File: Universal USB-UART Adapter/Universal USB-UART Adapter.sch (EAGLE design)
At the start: 9 parts, among them U1 FT232RQ, X1 USBPCB

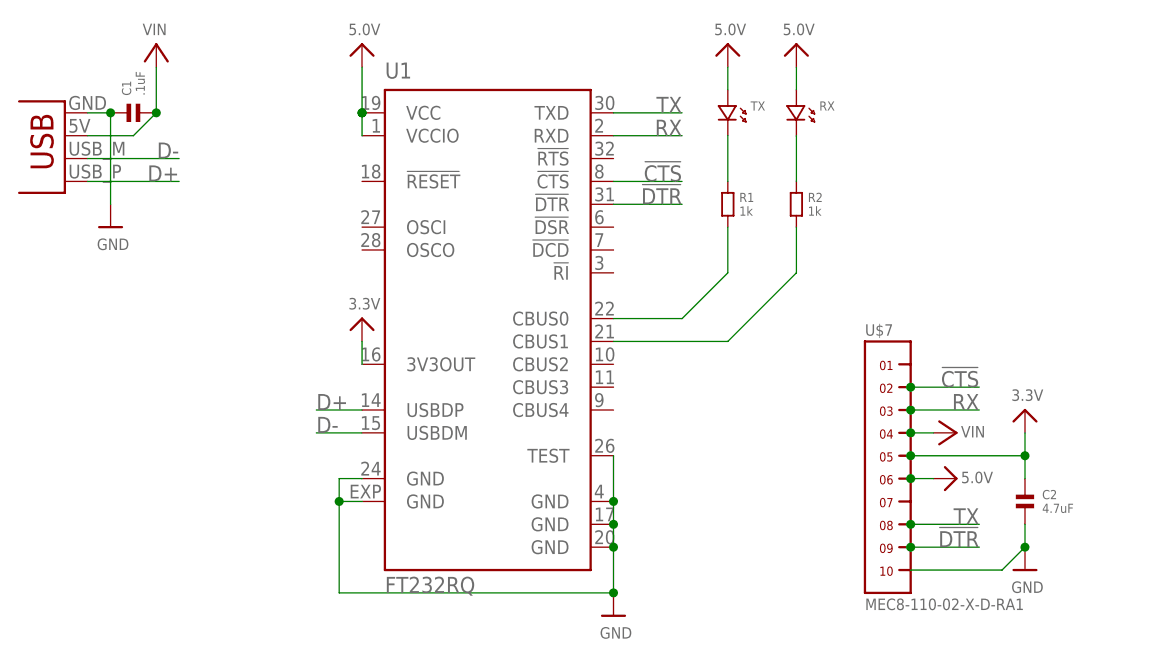
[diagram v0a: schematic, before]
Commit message: Modified voltage connections to be next to each other. Easier to short.
Signed-off-by: Cruz Monrreal II <Cruz.Monrreal@gmail.com>
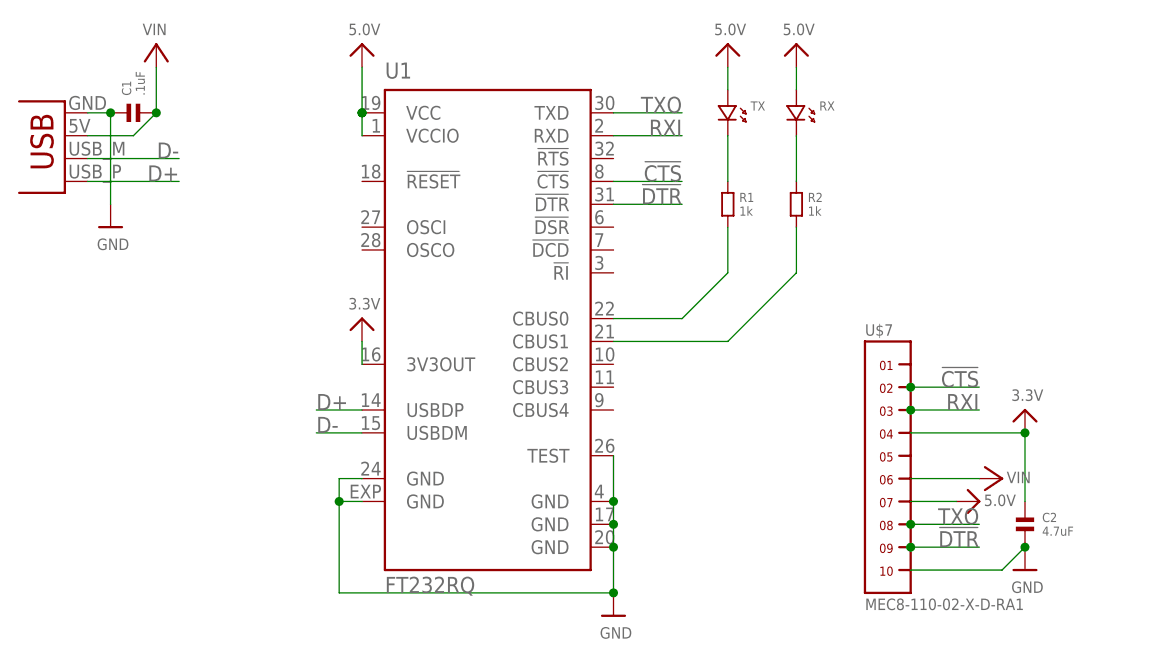
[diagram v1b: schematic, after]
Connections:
- net RX renamed RXI
- net TX renamed TXO
- net 3.3V: now also U$7.4; no longer U$7.5
- net 5.0V: now also U$7.7; no longer U$7.6
- net VIN: now also U$7.6; no longer U$7.4
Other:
- moved on the sheet: C2
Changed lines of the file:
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@@
 <instance part="TX" gate="G$1" x="93.98" y="154.94" rot="R270"/>
 <instance part="RX" gate="G$1" x="101.6" y="154.94" rot="R270"/>
-<instance part="U$3" gate="G$1" x="116.84" y="114.3" smashed="yes" rot="R270">
-<attribute name="VALUE" x="119.888" y="113.792" size="1.27" layer="96"/>
+<instance part="U$3" gate="G$1" x="119.38" y="111.76" smashed="yes" rot="R270">
+<attribute name="VALUE" x="122.428" y="111.252" size="1.27" layer="96"/>
 </instance>
 <instance part="C1" gate="G$1" x="27.94" y="154.94"/>
-<instance part="U$8" gate="G$1" x="116.84" y="119.38" smashed="yes" rot="R270">
-<attribute name="VALUE" x="119.888" y="118.872" size="1.27" layer="96"/>
+<instance part="U$8" gate="G$1" x="121.92" y="114.3" smashed="yes" rot="R270">
+<attribute name="VALUE" x="124.968" y="113.792" size="1.27" layer="96"/>
 </instance>
 <instance part="U$9" gate="G$1" x="30.48" y="160.02"/>
 <instance part="U$11" gate="G$1" x="127" y="119.38"/>
 <instance part="U$12" gate="G$1" x="127" y="104.14"/>
-<instance part="C2" gate="G$1" x="127" y="111.76" rot="R270"/>
+<instance part="C2" gate="G$1" x="127" y="109.22" rot="R270"/>
 </instances>
 <busses>
@@
 <wire x1="124.46" y1="104.14" x2="127" y2="106.68" width="0.1524" layer="91"/>
 <pinref part="C2" gate="G$1" pin="2"/>
-<wire x1="127" y1="106.68" x2="127" y2="109.22" width="0.1524" layer="91"/>
 <junction x="127" y="106.68"/>
 <pinref part="U$7" gate="G$1" pin="10"/>
@@
 </segment>
 </net>
-<net name="TX" class="0">
+<net name="TXO" class="0">
 <segment>
 <wire x1="81.28" y1="154.94" x2="88.9" y2="154.94" width="0.1524" layer="91"/>
@@
 </segment>
 </net>
-<net name="RX" class="0">
+<net name="RXI" class="0">
 <segment>
 <wire x1="88.9" y1="152.4" x2="81.28" y2="152.4" width="0.1524" layer="91"/>
@@
 <segment>
 <pinref part="U$11" gate="G$1" pin="3.3V"/>
-<wire x1="127" y1="116.84" x2="127" y2="119.38" width="0.1524" layer="91"/>
 <pinref part="C2" gate="G$1" pin="1"/>
-<wire x1="127" y1="114.3" x2="127" y2="116.84" width="0.1524" layer="91"/>
-<wire x1="127" y1="116.84" x2="114.3" y2="116.84" width="0.1524" layer="91"/>
-<junction x="127" y="116.84"/>
-<pinref part="U$7" gate="G$1" pin="5"/>
-<junction x="114.3" y="116.84"/>
+<wire x1="127" y1="111.76" x2="127" y2="119.38" width="0.1524" layer="91"/>
+<pinref part="U$7" gate="G$1" pin="4"/>
+<wire x1="114.3" y1="119.38" x2="127" y2="119.38" width="0.1524" layer="91"/>
+<junction x="127" y="119.38"/>
 </segment>
 <segment>
@@
 </segment>
 <segment>
-<wire x1="114.3" y1="114.3" x2="116.84" y2="114.3" width="0.1524" layer="91"/>
+<pinref part="U$7" gate="G$1" pin="7"/>
 <pinref part="U$3" gate="G$1" pin="5.0V"/>
-<pinref part="U$7" gate="G$1" pin="6"/>
-<junction x="114.3" y="114.3"/>
+<wire x1="114.3" y1="111.76" x2="119.38" y2="111.76" width="0.1524" layer="91"/>
 </segment>
 </net>
@@
 </segment>
 <segment>
+<pinref part="U$7" gate="G$1" pin="6"/>
 <pinref part="U$8" gate="G$1" pin="VIN"/>
-<pinref part="U$7" gate="G$1" pin="4"/>
-<junction x="114.3" y="119.38"/>
-<wire x1="114.3" y1="119.38" x2="116.84" y2="119.38" width="0.1524" layer="91"/>
-</segment>
-</net>
+<wire x1="114.3" y1="114.3" x2="121.92" y2="114.3" width="0.1524" layer="91"/>
+</segment>
+</net>

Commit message: Changed connector to 2mm pitch as opposed to PCB connector
Signed-off-by: Cruz Monrreal II <Cruz.Monrreal@gmail.com>
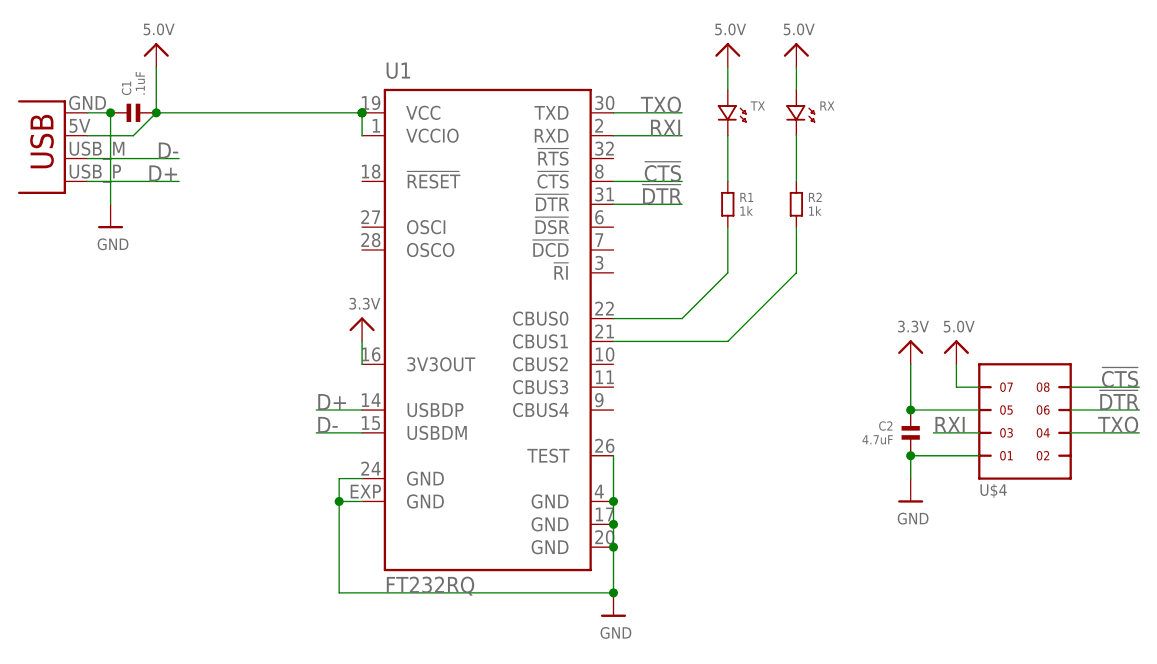
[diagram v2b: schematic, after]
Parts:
- removed U$7: MEC8-110-02-X-D-RA1, samtec:MEC8-110-02-X-D-RA1
- added U$4: (no value), samtec:MMT-104-01-X-DH-X
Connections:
- removed net VIN: C1.2, U$7.6, X1.VBUS
- net !CTS: now also U$4.8; no longer U$7.2
- net !DTR: now also U$4.6; no longer U$7.9
- net 3.3V: now also U$4.5; no longer U$7.4
- net 5.0V: now also C1.2, U$4.7, X1.VBUS; no longer U$7.7
- net GND: now also U$4.1; no longer U$7.10
- net RXI: now also U$4.3; no longer U$7.3
- net TXO: now also U$4.4; no longer U$7.8
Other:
- moved on the sheet: C2
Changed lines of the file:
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@@
 <part name="U$15" library="microbuilder" deviceset="5.0V" device=""/>
 <part name="U$6" library="microbuilder" deviceset="5.0V" device=""/>
-<part name="U$7" library="samtec" deviceset="MEC8-110-02-X-D-RA1" device=""/>
 <part name="R1" library=".standardparts" deviceset="RESISTOR" device=".0603" value="1k"/>
 <part name="R2" library=".standardparts" deviceset="RESISTOR" device=".0603" value="1k"/>
@@
 <part name="U$3" library="microbuilder" deviceset="5.0V" device=""/>
 <part name="C1" library=".standardparts" deviceset="CAPACITOR" device=".0603" value=".1uF"/>
-<part name="U$8" library="microbuilder" deviceset="VIN" device=""/>
-<part name="U$9" library="microbuilder" deviceset="VIN" device=""/>
 <part name="U$11" library="microbuilder" deviceset="3.3V" device=""/>
 <part name="U$12" library="microbuilder" deviceset="GND" device=""/>
 <part name="C2" library=".standardparts" deviceset="CAPACITOR" device=".0603" value="4.7uF"/>
+<part name="U$4" library="samtec" deviceset="MMT-104-01-X-DH-X" device=""/>
 </parts>
 <sheets>
@@
 <instance part="U$14" gate="G$1" x="101.6" y="160.02"/>
 <instance part="U$15" gate="G$1" x="93.98" y="160.02"/>
-<instance part="U$6" gate="G$1" x="53.34" y="160.02"/>
-<instance part="U$7" gate="G$1" x="111.76" y="116.84"/>
+<instance part="U$6" gate="G$1" x="30.48" y="160.02"/>
 <instance part="R1" gate="G$1" x="93.98" y="144.78" rot="R270"/>
 <instance part="R2" gate="G$1" x="101.6" y="144.78" rot="R270"/>
 <instance part="TX" gate="G$1" x="93.98" y="154.94" rot="R270"/>
 <instance part="RX" gate="G$1" x="101.6" y="154.94" rot="R270"/>
-<instance part="U$3" gate="G$1" x="119.38" y="111.76" smashed="yes" rot="R270">
-<attribute name="VALUE" x="122.428" y="111.252" size="1.27" layer="96"/>
+<instance part="U$3" gate="G$1" x="119.38" y="127"/>
+<instance part="C1" gate="G$1" x="27.94" y="154.94"/>
+<instance part="U$11" gate="G$1" x="114.3" y="127"/>
+<instance part="U$12" gate="G$1" x="114.3" y="111.76"/>
+<instance part="C2" gate="G$1" x="114.3" y="119.38" rot="MR270"/>
+<instance part="U$4" gate="G$1" x="127" y="121.92" smashed="yes" rot="MR180">
+<attribute name="NAME" x="121.92" y="113.665" size="1.27" layer="95" font="vector" rot="MR180"/>
+<attribute name="VALUE" x="121.92" y="128.905" size="1.27" layer="96" font="vector" rot="MR180"/>
 </instance>
-<instance part="C1" gate="G$1" x="27.94" y="154.94"/>
-<instance part="U$8" gate="G$1" x="121.92" y="114.3" smashed="yes" rot="R270">
-<attribute name="VALUE" x="124.968" y="113.792" size="1.27" layer="96"/>
-</instance>
-<instance part="U$9" gate="G$1" x="30.48" y="160.02"/>
-<instance part="U$11" gate="G$1" x="127" y="119.38"/>
-<instance part="U$12" gate="G$1" x="127" y="104.14"/>
-<instance part="C2" gate="G$1" x="127" y="109.22" rot="R270"/>
 </instances>
 <busses>
@@
 <segment>
 <pinref part="U$12" gate="G$1" pin="GND"/>
-<wire x1="114.3" y1="104.14" x2="124.46" y2="104.14" width="0.1524" layer="91"/>
-<wire x1="124.46" y1="104.14" x2="127" y2="106.68" width="0.1524" layer="91"/>
 <pinref part="C2" gate="G$1" pin="2"/>
-<junction x="127" y="106.68"/>
-<pinref part="U$7" gate="G$1" pin="10"/>
+<wire x1="114.3" y1="114.3" x2="114.3" y2="116.84" width="0.1524" layer="91"/>
+<pinref part="U$4" gate="G$1" pin="1"/>
+<wire x1="114.3" y1="116.84" x2="121.92" y2="116.84" width="0.1524" layer="91"/>
+<junction x="114.3" y="116.84"/>
 </segment>
 </net>
@@
 </segment>
 <segment>
-<wire x1="114.3" y1="109.22" x2="121.92" y2="109.22" width="0.1524" layer="91"/>
-<label x="121.92" y="109.22" size="1.778" layer="95" rot="MR0"/>
-<pinref part="U$7" gate="G$1" pin="8"/>
-<junction x="114.3" y="109.22"/>
+<wire x1="139.7" y1="119.38" x2="132.08" y2="119.38" width="0.1524" layer="91"/>
+<label x="139.7" y="119.38" size="1.778" layer="95" rot="MR0"/>
+<pinref part="U$4" gate="G$1" pin="4"/>
 </segment>
 </net>
@@
 </segment>
 <segment>
-<label x="121.92" y="121.92" size="1.778" layer="95" rot="MR0"/>
-<pinref part="U$7" gate="G$1" pin="3"/>
-<junction x="114.3" y="121.92"/>
-<wire x1="114.3" y1="121.92" x2="121.92" y2="121.92" width="0.1524" layer="91"/>
+<label x="116.84" y="119.38" size="1.778" layer="95"/>
+<wire x1="116.84" y1="119.38" x2="121.92" y2="119.38" width="0.1524" layer="91"/>
+<pinref part="U$4" gate="G$1" pin="3"/>
 </segment>
 </net>
 <net name="3.3V" class="0">
-<segment>
-<pinref part="U$11" gate="G$1" pin="3.3V"/>
-<pinref part="C2" gate="G$1" pin="1"/>
-<wire x1="127" y1="111.76" x2="127" y2="119.38" width="0.1524" layer="91"/>
-<pinref part="U$7" gate="G$1" pin="4"/>
-<wire x1="114.3" y1="119.38" x2="127" y2="119.38" width="0.1524" layer="91"/>
-<junction x="127" y="119.38"/>
-</segment>
 <segment>
 <pinref part="U1" gate="1" pin="3V3OUT"/>
@@
 <wire x1="53.34" y1="127" x2="53.34" y2="129.54" width="0.1524" layer="91"/>
 </segment>
+<segment>
+<pinref part="U$4" gate="G$1" pin="5"/>
+<wire x1="121.92" y1="121.92" x2="114.3" y2="121.92" width="0.1524" layer="91"/>
+<pinref part="U$11" gate="G$1" pin="3.3V"/>
+<wire x1="114.3" y1="121.92" x2="114.3" y2="127" width="0.1524" layer="91"/>
+<pinref part="C2" gate="G$1" pin="1"/>
+<junction x="114.3" y="121.92"/>
+</segment>
 </net>
 <net name="!DTR" class="0">
@@
 </segment>
 <segment>
-<wire x1="114.3" y1="106.68" x2="121.92" y2="106.68" width="0.1524" layer="91"/>
-<label x="121.92" y="106.68" size="1.778" layer="95" rot="MR0"/>
-<pinref part="U$7" gate="G$1" pin="9"/>
-<junction x="114.3" y="106.68"/>
+<wire x1="132.08" y1="121.92" x2="139.7" y2="121.92" width="0.1524" layer="91"/>
+<label x="139.7" y="121.92" size="1.778" layer="95" rot="MR0"/>
+<pinref part="U$4" gate="G$1" pin="6"/>
 </segment>
 </net>
@@
 <segment>
 <pinref part="U$6" gate="G$1" pin="5.0V"/>
-<wire x1="53.34" y1="160.02" x2="53.34" y2="154.94" width="0.1524" layer="91"/>
 <junction x="53.34" y="154.94"/>
 <junction x="53.34" y="154.94"/>
@@
 <wire x1="53.34" y1="152.4" x2="53.34" y2="154.94" width="0.1524" layer="91"/>
 <pinref part="U1" gate="1" pin="VCCIO"/>
+<wire x1="22.86" y1="152.4" x2="27.94" y2="152.4" width="0.1524" layer="91"/>
+<wire x1="30.48" y1="154.94" x2="27.94" y2="152.4" width="0.1524" layer="91"/>
+<pinref part="X1" gate="G$1" pin="VBUS"/>
+<pinref part="C1" gate="G$1" pin="2"/>
+<wire x1="30.48" y1="154.94" x2="53.34" y2="154.94" width="0.1524" layer="91"/>
+<junction x="30.48" y="154.94"/>
+<wire x1="30.48" y1="154.94" x2="30.48" y2="160.02" width="0.1524" layer="91"/>
 </segment>
 <segment>
@@
 </segment>
 <segment>
-<pinref part="U$7" gate="G$1" pin="7"/>
 <pinref part="U$3" gate="G$1" pin="5.0V"/>
-<wire x1="114.3" y1="111.76" x2="119.38" y2="111.76" width="0.1524" layer="91"/>
+<wire x1="119.38" y1="124.46" x2="119.38" y2="127" width="0.1524" layer="91"/>
+<pinref part="U$4" gate="G$1" pin="7"/>
+<wire x1="119.38" y1="124.46" x2="121.92" y2="124.46" width="0.1524" layer="91"/>
 </segment>
 </net>
@@
 </segment>
 <segment>
-<wire x1="114.3" y1="124.46" x2="121.92" y2="124.46" width="0.1524" layer="91"/>
-<label x="121.92" y="124.46" size="1.778" layer="95" rot="MR0"/>
-<pinref part="U$7" gate="G$1" pin="2"/>
-<junction x="114.3" y="124.46"/>
+<wire x1="139.7" y1="124.46" x2="132.08" y2="124.46" width="0.1524" layer="91"/>
+<label x="139.7" y="124.46" size="1.778" layer="95" rot="MR0"/>
+<pinref part="U$4" gate="G$1" pin="8"/>
 </segment>
 </net>
@@
 </segment>
 </net>
-<net name="VIN" class="0">
-<segment>
-<wire x1="22.86" y1="152.4" x2="27.94" y2="152.4" width="0.1524" layer="91"/>
-<wire x1="30.48" y1="154.94" x2="27.94" y2="152.4" width="0.1524" layer="91"/>
-<pinref part="X1" gate="G$1" pin="VBUS"/>
-<pinref part="C1" gate="G$1" pin="2"/>
-<junction x="30.48" y="154.94"/>
-<pinref part="U$9" gate="G$1" pin="VIN"/>
-<wire x1="30.48" y1="154.94" x2="30.48" y2="160.02" width="0.1524" layer="91"/>
-</segment>
-<segment>
-<pinref part="U$7" gate="G$1" pin="6"/>
-<pinref part="U$8" gate="G$1" pin="VIN"/>
-<wire x1="114.3" y1="114.3" x2="121.92" y2="114.3" width="0.1524" layer="91"/>
-</segment>
-</net>
